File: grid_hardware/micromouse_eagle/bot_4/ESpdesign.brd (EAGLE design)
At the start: 89.8 x 61 mm, 8 parts

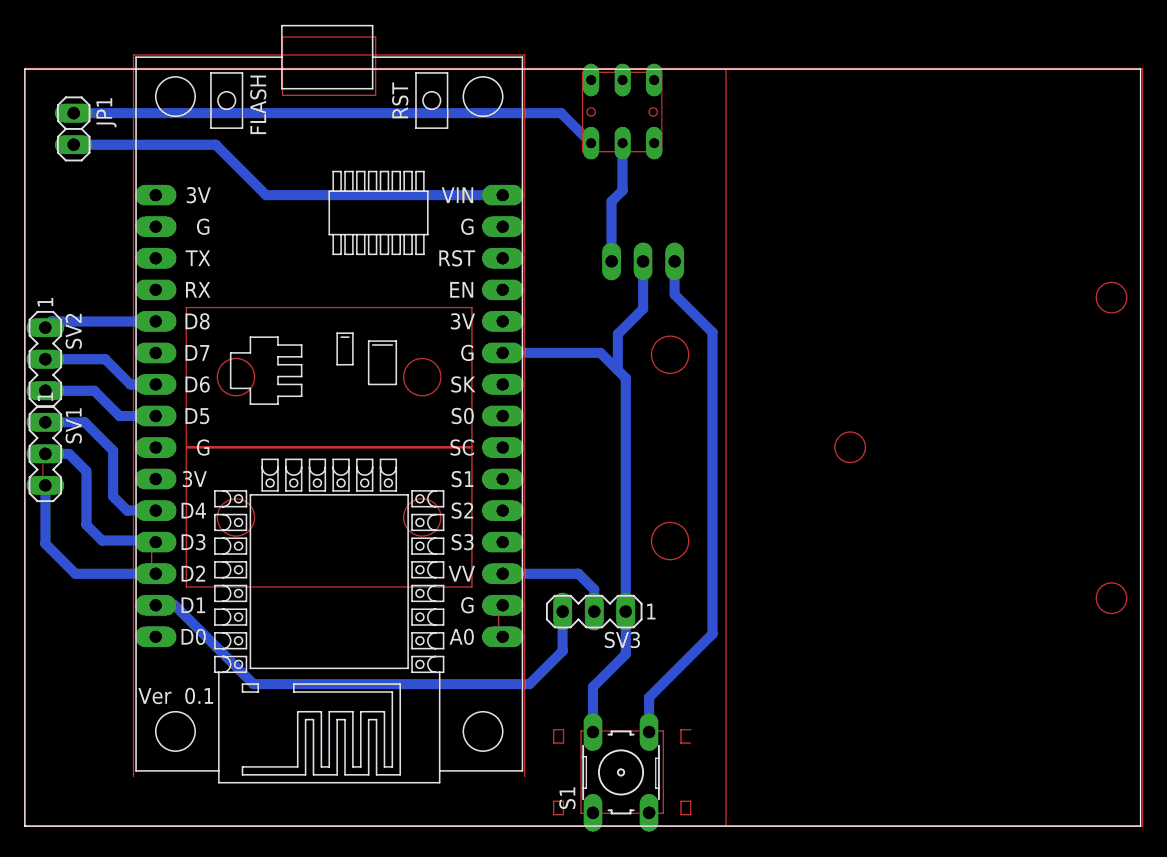
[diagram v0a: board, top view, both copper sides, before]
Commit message: sch, brd of 123 and 4th bot changed
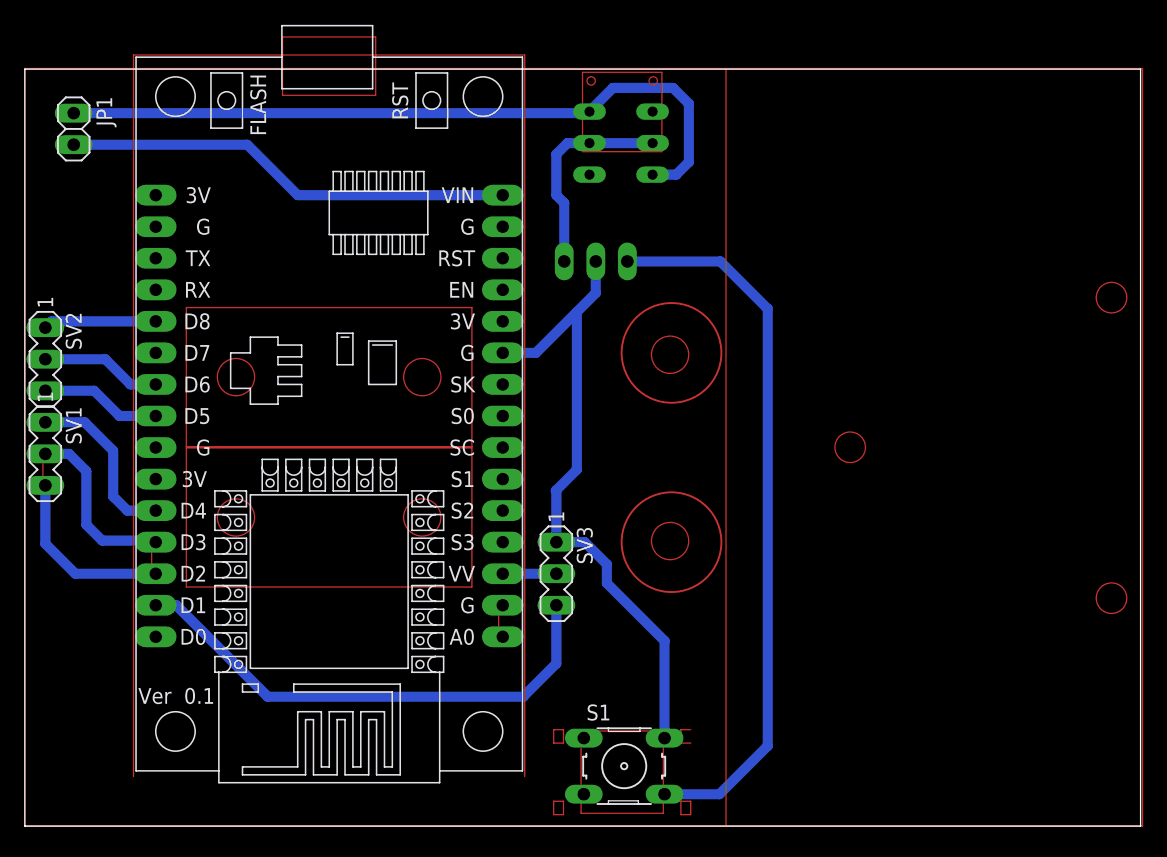
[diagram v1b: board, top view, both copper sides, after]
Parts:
- moved SV3 4.31 mm to (42.8, 20.3), turned to 270 degrees
- moved SV4 3.81 mm to (46.0, 45.5)
- moved S2 2.54 mm to (48.0, 55.0), turned to 270 degrees
- moved S1 0.57 mm to (48.3, 4.83), turned to 0 degrees
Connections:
- net P+: now also S2.5, S2.6
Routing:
- net P+: track 52.5 -> 76.2 mm
- net B-: track 41.3 -> 58.0 mm
- net 5V: track 45.9 -> 40.5 mm
- net GND: track 51.3 -> 53.1 mm
- net D1: track 39.7 -> 41.1 mm
